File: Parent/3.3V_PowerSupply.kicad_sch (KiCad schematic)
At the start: 1 part, among them U63 LD1117S33TR_SOT223

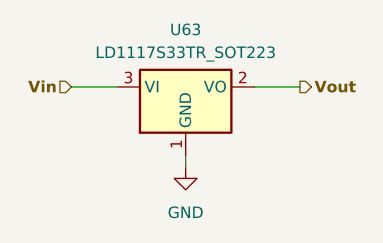
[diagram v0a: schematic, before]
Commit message: Updated Parent - Moved workspace to cloud
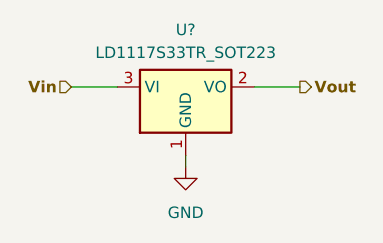
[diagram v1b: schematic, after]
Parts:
- renumbered U63 to U?
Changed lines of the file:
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@@
   (symbol (lib_id "Regulator_Linear:LD1117S33TR_SOT223") (at 144.78 62.23 0) (unit 1)
     (in_bom yes) (on_board yes) (dnp no) (fields_autoplaced)
-    (property "Reference" "U63" (at 144.78 55.88 0)
+    (property "Reference" "U?" (at 144.78 55.88 0)
       (effects (font (size 1.27 1.27)))
     )
@@
       (project "Parent"
         (path "/1451ec1d-c665-471b-ba41-1d89ef6a63bf/0b8ceb61-553b-4ac5-8229-ed236c1b50ba"
-          (reference "U63") (unit 1)
+          (reference "U?") (unit 1)
         )
       )
@@
   (symbol (lib_id "power:GND") (at 144.78 71.12 0) (unit 1)
     (in_bom yes) (on_board yes) (dnp no) (fields_autoplaced)
-    (property "Reference" "#PWR030" (at 144.78 77.47 0)
+    (property "Reference" "#PWR?" (at 144.78 77.47 0)
       (effects (font (size 1.27 1.27)) hide)
     )
@@
       (project "Parent"
         (path "/1451ec1d-c665-471b-ba41-1d89ef6a63bf/7708e5b2-0a75-40c8-a3d2-8281cd192259"
-          (reference "#PWR030") (unit 1)
+          (reference "#PWR?") (unit 1)
         )
         (path "/1451ec1d-c665-471b-ba41-1d89ef6a63bf/0b8ceb61-553b-4ac5-8229-ed236c1b50ba"
-          (reference "#PWR030") (unit 1)
+          (reference "#PWR?") (unit 1)
         )
       )
